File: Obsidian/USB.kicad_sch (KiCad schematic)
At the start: 40 parts, among them J2 USB_C_Receptacle_USB2.0_16P, U21 FT2232HQ, U22 93C46B-I_SN, U8 TLV62565DBV, Y5 XTAL_12MHZ_TXC_7A-12.000MAAJ-T

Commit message: update with available components on LCSC
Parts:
- C70, C74, C75, C76, C77, C78, C79, C80, C82, C84, C86, C88: LCSC (none) -> C110251
- C71, C72: LCSC (none) -> C1557
- C73, C81, C85, C87: LCSC (none) -> C318563
- C83: LCSC (none) -> C296720
- D1: FT Rotation Offset (none) -> 270; LCSC (none) -> C5158049
- J2: LCSC (none) -> C3020560
- L10, L12, L13: FT Rotation Offset (none) -> 0; LCSC (none) -> C88970
- L14: FT Rotation Offset (none) -> 0; LCSC (none) -> C5832344
- R74, R83: LCSC (none) -> C2906865
- R75, R76, R77, R81: LCSC (none) -> C60490
- R78: LCSC (none) -> C2909316
- R79: LCSC (none) -> C25900
- R80, R82: LCSC (none) -> C25905
- U21: FT Rotation Offset (none) -> 0; LCSC (none) -> C193662
- U22: LCSC (none) -> C1348804
- U8: FT Rotation Offset (none) -> 180; LCSC (none) -> C87122
- Y5: LCSC (none) -> C112573

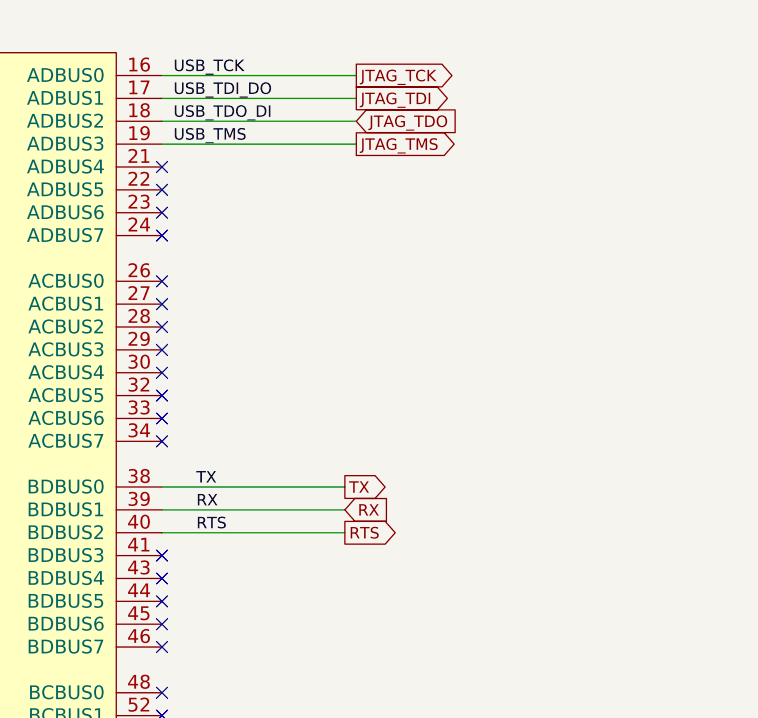
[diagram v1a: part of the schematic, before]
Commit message: replacing global label with hierarchical label
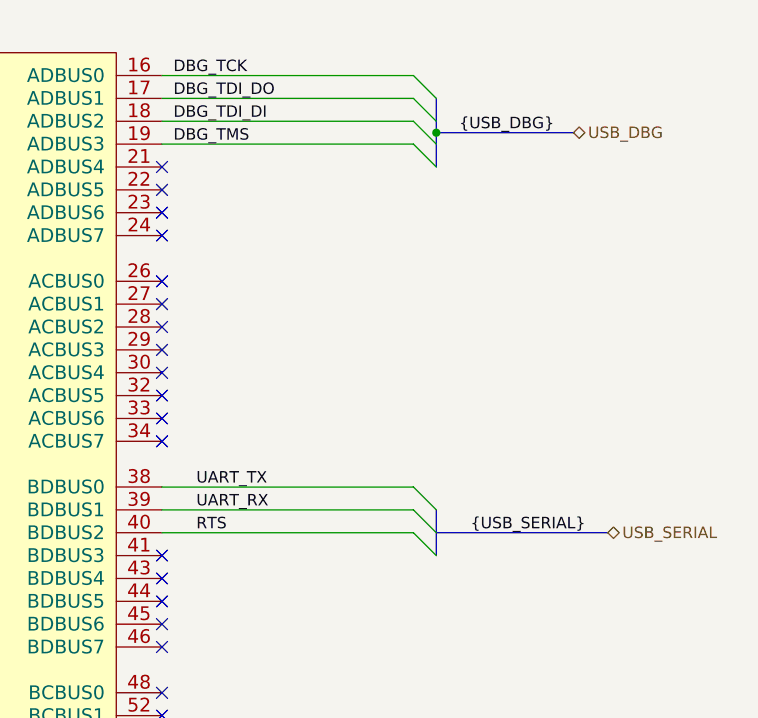
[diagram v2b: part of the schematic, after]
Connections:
- net JTAG_TCK renamed DBG_TCK
- net JTAG_TDI renamed DBG_TDI_DO
- net JTAG_TDO renamed DBG_TDI_DI
- net JTAG_TMS renamed DBG_TMS
- net RX renamed UART_RX
- net TX renamed UART_TX

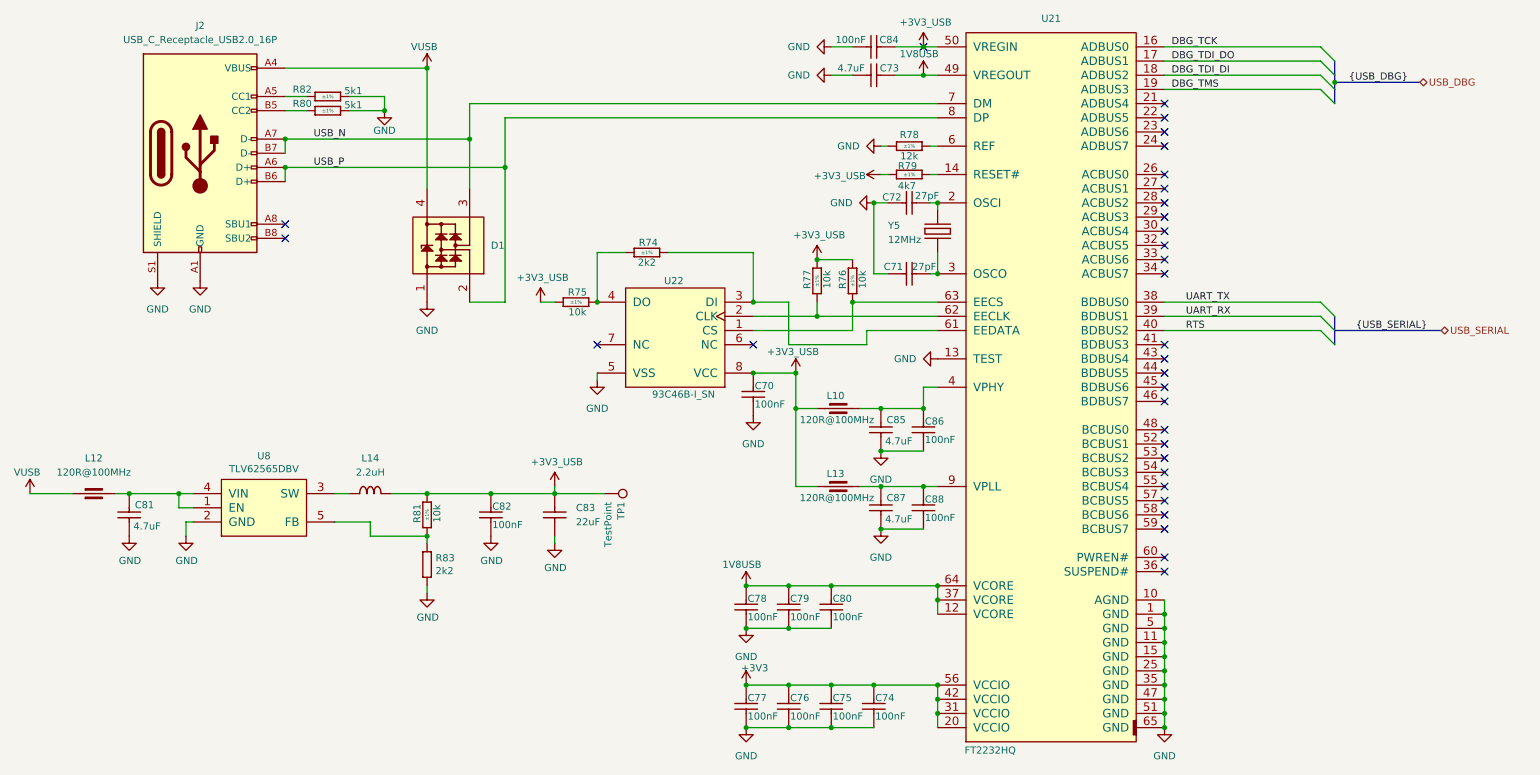
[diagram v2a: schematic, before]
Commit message: Adding symbol library
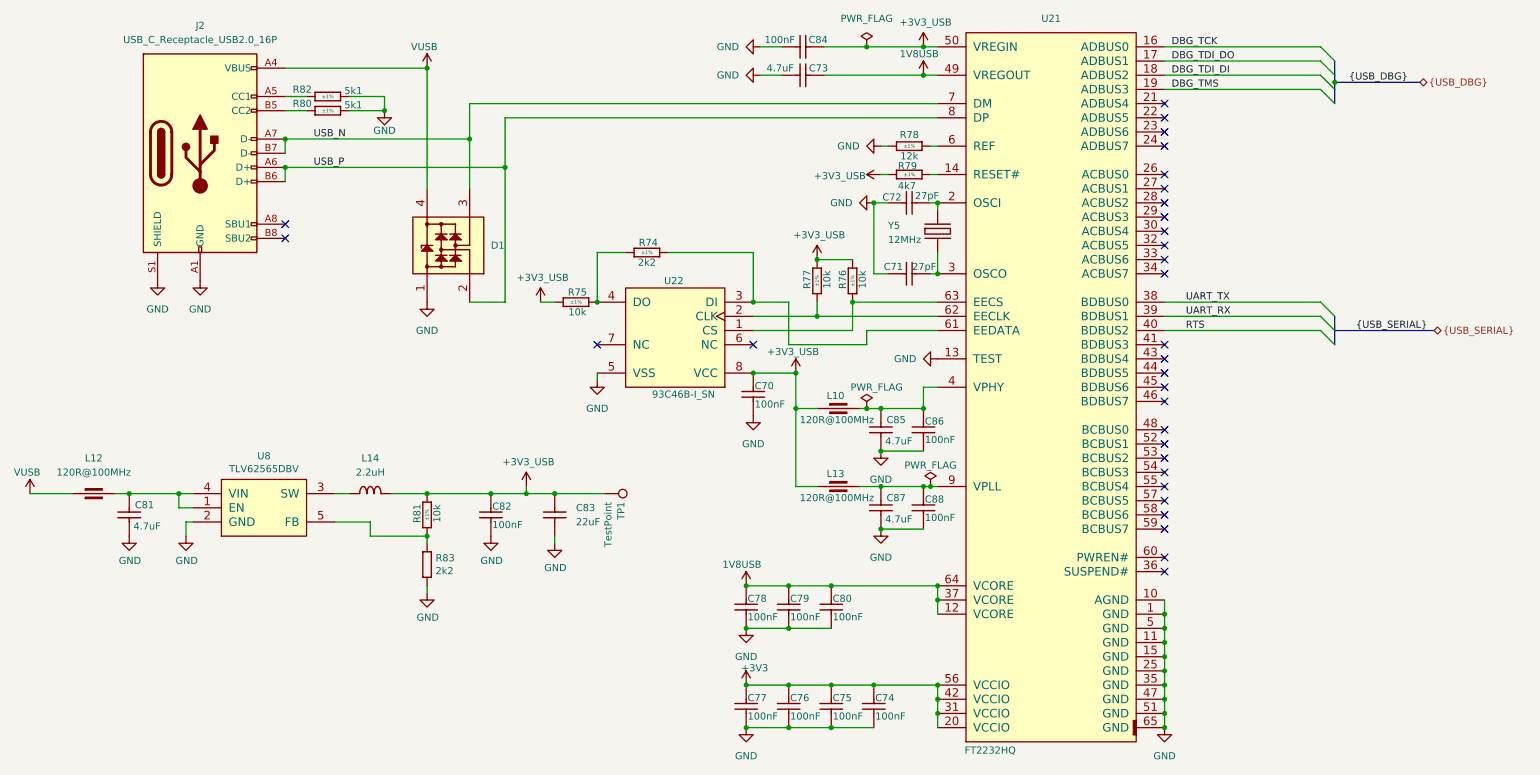
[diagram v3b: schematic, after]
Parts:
- C70, C74, C75, C76, C77, C78, C79, C80, C82, C84, C86, C88: symbol Capacitors SMD:CC0402_100NF_50V_10%_X7R -> Library_Symbol:CC0402_100NF_50V_10%_X7R
- C71, C72: symbol Capacitors SMD:CC0402_27PF_50V_5%_C0G -> Library_Symbol:CC0402_27PF_50V_5%_C0G
- C73, C81, C85, C87: symbol Capacitors SMD:CC0402_4.7UF_16V_20%_X5R -> Library_Symbol:CC0402_4.7UF_16V_20%_X5R
- C83: symbol Capacitors SMD:CC0805_22UF_16V_10%_X5R -> Library_Symbol:CC0805_22UF_16V_10%_X5R
- D1: symbol Diodes:PRTR5V0U2X -> Library_Symbol:PRTR5V0U2X
- J2: symbol Connector:USB_C_Receptacle_USB2.0_16P -> Library_Symbol:USB_C_Receptacle_USB2.0_16P
- L10, L12, L13: symbol Inductors SMD:IND0402_MURATA_BLM15PX121SN1D -> Library_Symbol:IND0402_MURATA_BLM15PX121SN1D
- L14: symbol Inductors SMD:IND_2.2UH_20%_WURTH_WE-PMCI_74479276222C -> Library_Symbol:IND_2.2UH_20%_WURTH_WE-PMCI_74479276222C
- R74: symbol Resistors SMD:R0402_2K2_1%_0.0625W_100PPM -> Library_Symbol:R0402_2K2_1%_0.0625W_100PPM
- R75, R76, R77, R81: symbol Resistors SMD:R0402_10K_1%_0.0625W_100PPM -> Library_Symbol:R0402_10K_1%_0.0625W_100PPM
- R78: symbol Resistors SMD:R0402_12K_1%_0.0625W_100PPM -> Library_Symbol:R0402_12K_1%_0.0625W_100PPM
- R79: symbol Resistors SMD:R0402_4K7_1%_0.0625W_100PPM -> Library_Symbol:R0402_4K7_1%_0.0625W_100PPM
- R80, R82: symbol Resistors SMD:R0402_5K1_1%_0.0625W_100PPM -> Library_Symbol:R0402_5K1_1%_0.0625W_100PPM
- R83: symbol Resistors_SMD:R0402_2K2_1%_0.0625W_100PPM -> Library_Symbol:R0402_2K2_1%_0.0625W_100PPM
- TP1: symbol Connector_Generic:TestPoint -> Library_Symbol:TestPoint
- U21: symbol Analog & Interface:FT2232HQ -> Library_Symbol:FT2232HQ
- U22: symbol Logic:93C46B-I_SN -> Library_Symbol:93C46B-I_SN
- U8: symbol Regulators:TLV62565DBV -> Library_Symbol:TLV62565DBV
- Y5: symbol Crystals & Oscillators:XTAL_12MHZ_TXC_7A-12.000MAAJ-T -> Library_Symbol:XTAL_12MHZ_TXC_7A-12.000MAAJ-T
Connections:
- no-connect marks 32 -> 31
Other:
- moved on the sheet: C73, C84

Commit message: Correct Schematic errors
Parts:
- C70, C71, C72, C73, C74, C75, C76, C77, C78, C79, C80, C81, C82, C84, C85, C86, C87, C88: footprint Capacitors SMD:CAPC1005X55N -> Footprint:CAPC1005X55N
- C83: footprint Capacitors SMD:CAPC2012X135N -> Footprint:CAPC2012X135N
- D1: footprint ICs And Semiconductors SMD:SOT190P230X110-4N -> Footprint:SOT190P230X110-4N
- J2: footprint Connector_USB:USB_C_Receptacle_GCT_USB4105-xx-A_16P_TopMnt_Horizontal -> Footprint:USB_C_Receptacle_GCT_USB4105-xx-A_16P_TopMnt_Horizontal
- L10, L12, L13: footprint Inductors SMD:INDC1005X55N -> Footprint:INDC1005X55N
- L14: footprint Inductors SMD:IND_WURTH_WE-PMCI_0806LR -> Footprint:IND_WURTH_WE-PMCI_0806LR
- R74, R75, R76, R77, R78, R79, R80, R81, R82: footprint Resistors SMD:RESC1005X40N -> Footprint:RESC1005X40N
- R83: footprint RESC1005X40N -> Footprint:RESC1005X40N; Database Table Name (none) -> Resistors; Footprint Library (none) -> Resistors SMD; HelpURL (none) -> \\cern.ch\dfs\Applications\Altium\Datasheets\R0402_Phycomp_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
- U21: footprint ICs And Semiconductors SMD:QFN50P900X900X100-65N-S445 -> Footprint:QFN50P900X900X100-65N-S445
- U22: footprint ICs And Semiconductors SMD:SOIC127P600X175-8N -> Footprint:SOIC127P600X175-8N
- U8: footprint ICs And Semiconductors SMD:SOT95P280X145-5N -> Footprint:SOT95P280X145-5N
- Y5: footprint ICs And Semiconductors SMD:XTAL_TXC_7A -> Footprint:XTAL_TXC_7A
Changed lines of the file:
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@@
 			)
 		)
-		(property "Footprint" "Capacitors SMD:CAPC1005X55N"
+		(property "Footprint" "Footprint:CAPC1005X55N"
 			(at 156.718 95.25 0)
 			(effects
@@
 			)
 		)
-		(property "Footprint" "Capacitors SMD:CAPC1005X55N"
+		(property "Footprint" "Footprint:CAPC1005X55N"
 			(at 187.198 115.57 0)
 			(effects
@@
 			)
 		)
-		(property "Footprint" "Capacitors SMD:CAPC1005X55N"
+		(property "Footprint" "Footprint:CAPC1005X55N"
 			(at 163.068 151.13 0)
 			(effects
@@
 			)
 		)
-		(property "Footprint" "Capacitors SMD:CAPC1005X55N"
+		(property "Footprint" "Footprint:CAPC1005X55N"
 			(at 155.448 133.35 0)
 			(effects
@@
 			)
 		)
-		(property "Footprint" "Capacitors SMD:CAPC1005X55N"
+		(property "Footprint" "Footprint:CAPC1005X55N"
 			(at 155.448 151.13 0)
 			(effects
@@
 			)
 		)
-		(property "Footprint" "Capacitors SMD:CAPC1005X55N"
+		(property "Footprint" "Footprint:CAPC1005X55N"
 			(at 180.34 49.022 0)
 			(effects
@@
 			)
 		)
-		(property "Footprint" "Capacitors SMD:CAPC1005X55N"
+		(property "Footprint" "Footprint:CAPC1005X55N"
 			(at 109.728 116.84 0)
 			(effects
@@
 			)
 		)
-		(property "Footprint" "Resistors SMD:RESC1005X40N"
+		(property "Footprint" "Footprint:RESC1005X40N"
 			(at 113.03 81.788 0)
 			(effects
@@
 			)
 		)
-		(property "Footprint" "Capacitors SMD:CAPC1005X55N"
+		(property "Footprint" "Footprint:CAPC1005X55N"
 			(at 180.34 61.722 0)
 			(effects
@@
 			)
 		)
-		(property "Footprint" "Resistors SMD:RESC1005X40N"
+		(property "Footprint" "Footprint:RESC1005X40N"
 			(at 97.028 116.84 0)
 			(effects
@@
 			)
 		)
-		(property "Footprint" "Capacitors SMD:CAPC2012X135N"
+		(property "Footprint" "Footprint:CAPC2012X135N"
 			(at 121.158 116.84 0)
 			(effects
@@
 			)
 		)
-		(property "Footprint" "Capacitors SMD:CAPC1005X55N"
+		(property "Footprint" "Footprint:CAPC1005X55N"
 			(at 163.068 133.35 0)
 			(effects
@@
 			)
 		)
-		(property "Footprint" "Capacitors SMD:CAPC1005X55N"
+		(property "Footprint" "Footprint:CAPC1005X55N"
 			(at 161.29 21.082 0)
 			(effects
@@
 			)
 		)
-		(property "Footprint" "Resistors SMD:RESC1005X40N"
+		(property "Footprint" "Footprint:RESC1005X40N"
 			(at 166.878 74.93 0)
 			(effects
@@
 			)
 		)
-		(property "Footprint" "Resistors SMD:RESC1005X40N"
+		(property "Footprint" "Footprint:RESC1005X40N"
 			(at 173.228 74.93 0)
 			(effects
@@
 			)
 		)
-		(property "Footprint" "Resistors SMD:RESC1005X40N"
+		(property "Footprint" "Footprint:RESC1005X40N"
 			(at 125.73 72.898 0)
 			(effects
@@
 			)
 		)
-		(property "Footprint" "ICs And Semiconductors SMD:SOT95P280X145-5N"
+		(property "Footprint" "Footprint:SOT95P280X145-5N"
 			(at 53.34 144.526 0)
 			(effects
@@
 			)
 		)
-		(property "Footprint" "Inductors SMD:INDC1005X55N"
+		(property "Footprint" "Footprint:INDC1005X55N"
 			(at 160.02 114.808 0)
 			(effects
@@
 			)
 		)
-		(property "Footprint" "ICs And Semiconductors SMD:XTAL_TXC_7A"
+		(property "Footprint" "Footprint:XTAL_TXC_7A"
 			(at 172.72 66.04 0)
 			(effects
@@
 			)
 		)
-		(property "Footprint" "Capacitors SMD:CAPC1005X55N"
+		(property "Footprint" "Footprint:CAPC1005X55N"
 			(at 170.688 133.35 0)
 			(effects
@@
 			)
 		)
-		(property "Footprint" "Resistors SMD:RESC1005X40N"
+		(property "Footprint" "Footprint:RESC1005X40N"
 			(at 68.58 47.498 0)
 			(effects
@@
 			)
 		)
-		(property "Footprint" "Capacitors SMD:CAPC1005X55N"
+		(property "Footprint" "Footprint:CAPC1005X55N"
 			(at 179.578 115.57 0)
 			(effects
@@
 			)
 		)
-		(property "Footprint" "Capacitors SMD:CAPC1005X55N"
+		(property "Footprint" "Footprint:CAPC1005X55N"
 			(at 178.308 151.13 0)
 			(effects
@@
 			)
 		)
-		(property "Footprint" "Capacitors SMD:CAPC1005X55N"
+		(property "Footprint" "Footprint:CAPC1005X55N"
 			(at 44.958 116.84 0)
 			(effects
@@
 			)
 		)
-		(property "Footprint" "ICs And Semiconductors SMD:SOIC127P600X175-8N"
+		(property "Footprint" "Footprint:SOIC127P600X175-8N"
 			(at 143.51 96.52 0)
 			(effects
@@
 			)
 		)
-		(property "Footprint" "Inductors SMD:INDC1005X55N"
+		(property "Footprint" "Footprint:INDC1005X55N"
 			(at 26.67 116.078 0)
 			(effects
@@
 			)
 		)
-		(property "Footprint" "Inductors SMD:INDC1005X55N"
+		(property "Footprint" "Footprint:INDC1005X55N"
 			(at 160.02 100.838 0)
 			(effects
@@
 			)
 		)
-		(property "Footprint" "Inductors SMD:IND_WURTH_WE-PMCI_0806LR"
+		(property "Footprint" "Footprint:IND_WURTH_WE-PMCI_0806LR"
 			(at 76.2 115.57 0)
 			(effects
@@
 			)
 		)
-		(property "Footprint" "ICs And Semiconductors SMD:QFN50P900X900X100-65N-S445"
+		(property "Footprint" "Footprint:QFN50P900X900X100-65N-S445"
 			(at 186.69 160.02 0)
 			(effects
@@
 			)
 		)
-		(property "Footprint" "Connector_USB:USB_C_Receptacle_GCT_USB4105-xx-A_16P_TopMnt_Horizontal"
+		(property "Footprint" "Footprint:USB_C_Receptacle_GCT_USB4105-xx-A_16P_TopMnt_Horizontal"
 			(at 53.34 48.26 0)
 			(effects
@@
 			)
 		)
-		(property "Footprint" "Capacitors SMD:CAPC1005X55N"
+		(property "Footprint" "Footprint:CAPC1005X55N"
 			(at 161.29 26.162 0)
 			(effects
@@
 			)
 		)
-		(property "Footprint" "ICs And Semiconductors SMD:SOT190P230X110-4N"
+		(property "Footprint" "Footprint:SOT190P230X110-4N"
 			(at 106.68 69.85 0)
 			(effects
@@
 			)
 		)
-		(property "Footprint" "Resistors SMD:RESC1005X40N"
+		(property "Footprint" "Footprint:RESC1005X40N"
 			(at 172.72 53.848 0)
 			(effects
@@
 			)
 		)
-		(property "Footprint" "RESC1005X40N"
+		(property "Footprint" "Footprint:RESC1005X40N"
 			(at 64.262 118.11 0)
 			(effects
@@
 			)
 		)
+		(property "Database Table Name" "Resistors"
+			(at 90.17 118.11 0)
+			(effects
+				(font
+					(size 1.27 1.27)
+				)
+				(hide yes)
+			)
+		)
+		(property "Footprint Library" "Resistors SMD"
+			(at 90.17 118.11 0)
+			(effects
+				(font
+					(size 1.27 1.27)
+				)
+				(hide yes)
+			)
+		)
+		(property "HelpURL" "\\\\cern.ch\\dfs\\Applications\\Altium\\Datasheets\\R0402_Phycomp_RC0402.pdf"
+			(at 90.17 118.11 0)
+			(effects
+				(font
+					(size 1.27 1.27)
+				)
+				(hide yes)
+			)
+		)
 		(pin "1"
 		)
@@
 			)
 		)
-		(property "Footprint" "Resistors SMD:RESC1005X40N"
+		(property "Footprint" "Footprint:RESC1005X40N"
 			(at 180.34 45.212 0)
 			(effects
@@
 			)
 		)
-		(property "Footprint" "Capacitors SMD:CAPC1005X55N"
+		(property "Footprint" "Footprint:CAPC1005X55N"
 			(at 179.578 101.6 0)
 			(effects
@@
 			)
 		)
-		(property "Footprint" "Resistors SMD:RESC1005X40N"
+		(property "Footprint" "Footprint:RESC1005X40N"
 			(at 68.58 44.958 0)
 			(effects
@@
 			)
 		)
-		(property "Footprint" "Capacitors SMD:CAPC1005X55N"
+		(property "Footprint" "Footprint:CAPC1005X55N"
 			(at 170.688 151.13 0)
 			(effects
@@
 			)
 		)
-		(property "Footprint" "Capacitors SMD:CAPC1005X55N"
+		(property "Footprint" "Footprint:CAPC1005X55N"
 			(at 187.198 101.6 0)
 			(effects

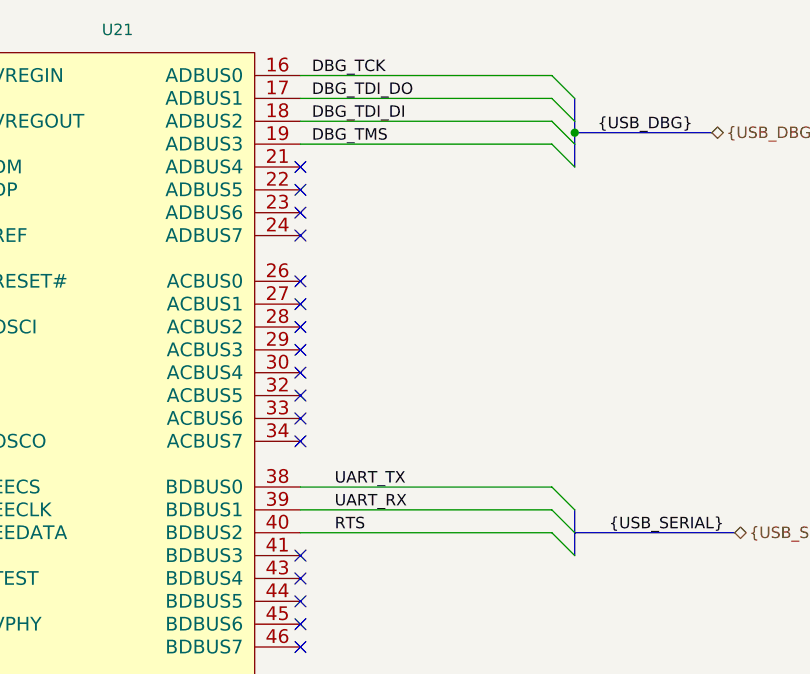
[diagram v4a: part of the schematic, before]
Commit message: correcting mismatch in TX/RX of UART
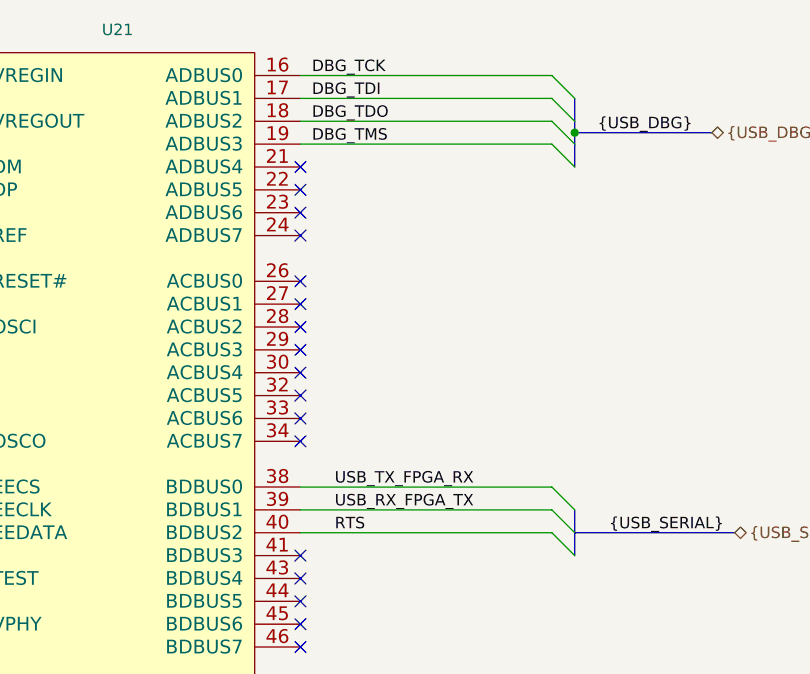
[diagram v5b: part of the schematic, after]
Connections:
- net DBG_TDI_DI renamed DBG_TDO
- net DBG_TDI_DO renamed DBG_TDI
- net UART_RX renamed USB_RX_FPGA_TX
- net UART_TX renamed USB_TX_FPGA_RX
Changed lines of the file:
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@@
 	)
 	(bus_alias "USB_DBG"
-		(members "DBG_TCK" "DBG_TDI_DO" "DBG_TDI_DI" "DBG_TMS")
+		(members "DBG_TCK" "DBG_TDI" "DBG_TDO" "DBG_TMS")
 	)
 	(bus_alias "USB_SERIAL"
-		(members "UART_TX" "UART_RX" "RTS")
+		(members "USB_TX_FPGA_RX" "USB_RX_FPGA_TX" "RTS")
 	)
 	(junction
@@
 		)
 	)
-	(label "UART_RX"
+	(label "USB_RX_FPGA_TX"
 		(at 226.06 77.47 0)
 		(effects
@@
 		)
 	)
-	(label "DBG_TDI_DI"
+	(label "DBG_TDO"
 		(at 223.52 34.29 0)
 		(effects
@@
 		)
 	)
-	(label "UART_TX"
+	(label "USB_TX_FPGA_RX"
 		(at 226.06 74.93 0)
 		(effects
@@
 		)
 	)
-	(label "DBG_TDI_DO"
+	(label "DBG_TDI"
 		(at 223.52 31.75 0)
 		(effects
